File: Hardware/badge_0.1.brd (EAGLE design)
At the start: 100 x 50 mm, 59 parts, among them CON1 PH_2, IC1 CP2102, SW2 MK12C02, U1 SMBT2222A, U2 SMBT2222A, U4 MCP73832T-2DCI/OT

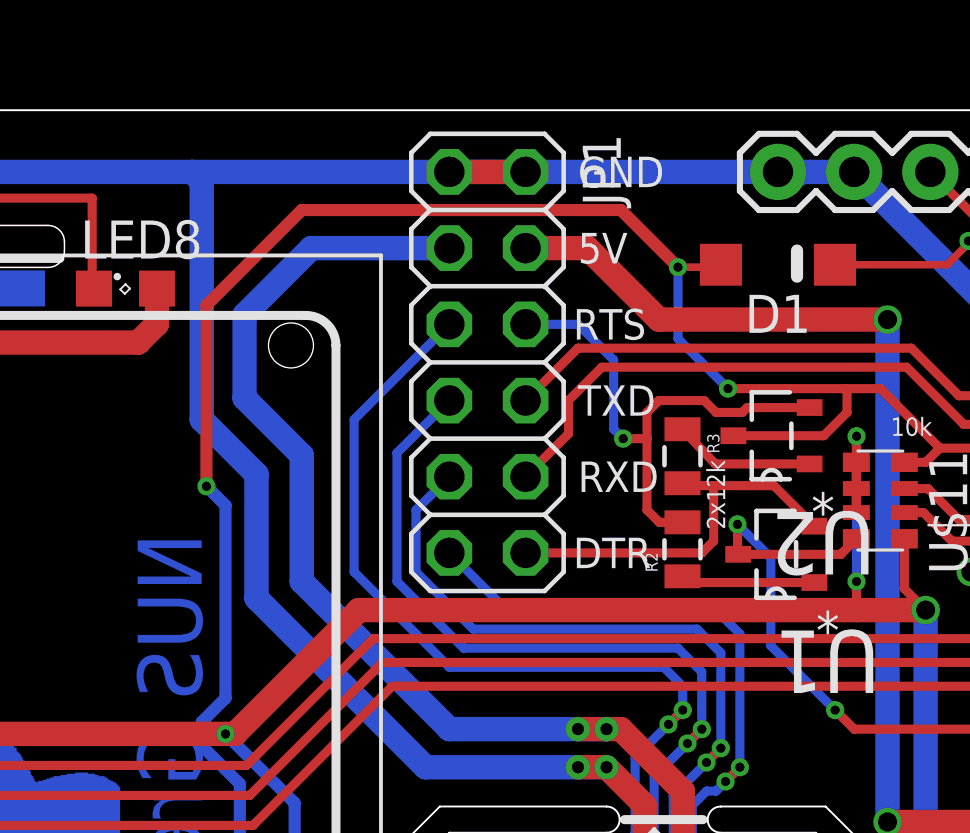
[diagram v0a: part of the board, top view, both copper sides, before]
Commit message: Replaced serial jumpers with a header. Thus removing the need to populate the jumpers during board assembly.
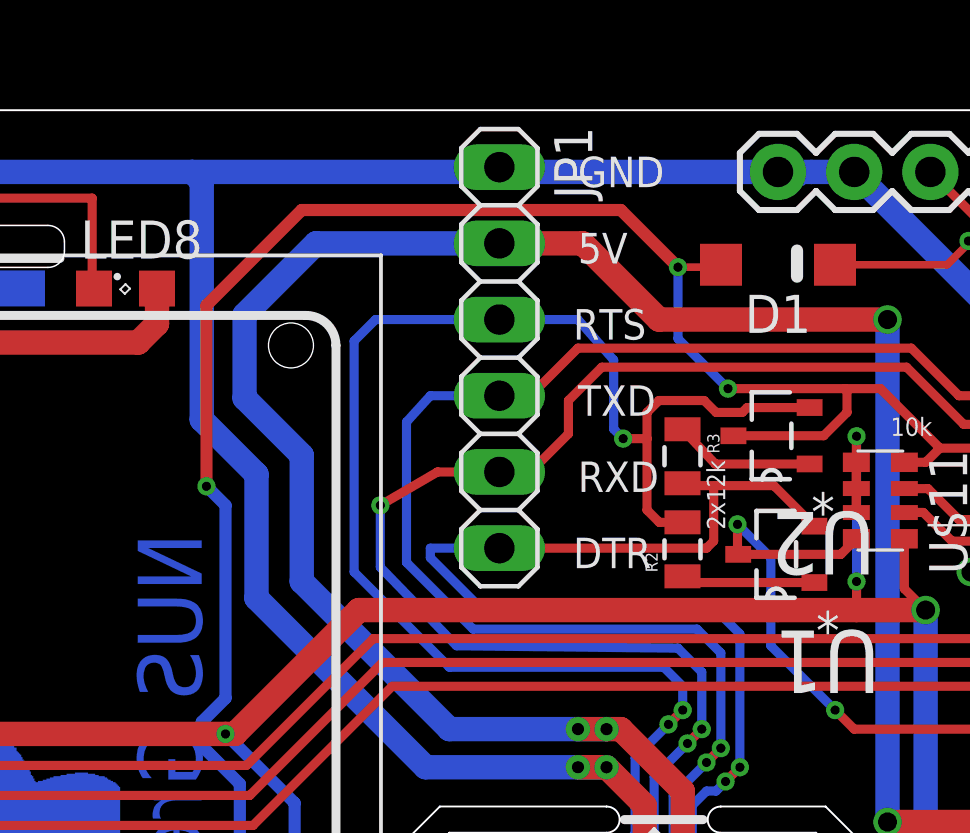
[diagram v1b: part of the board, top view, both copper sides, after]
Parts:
- JP1: device pinhead:2X06 -> pinhead:1X06
- moved JP1 0.43 mm to (45.5, 41.8)
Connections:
- removed net AUTO_DTR: JP1.12, R3.2, U1.2
- removed net AUTO_RTS: JP1.6, R2.2, U2.2
- removed net S_RXD: IC1.25, J2.6, JP1.9
- removed net S_TXD: IC1.26, J2.5, JP1.7
- net 5V: no longer JP1.4
- net GND: no longer JP1.2
- net RX: now also IC1.25, J2.6, JP1.4; no longer JP1.8
- net S_DTR: now also JP1.6, R3.2, U1.2; no longer JP1.11
- net S_RTS: now also JP1.3, R2.2, U2.2; no longer JP1.5
- net TX: now also IC1.26, J2.5, JP1.5; no longer JP1.10
- net VBUS: now also JP1.2; no longer JP1.3
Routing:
- net RX: track 83.3 -> 132.3 mm, vias 3 -> 6
- net TX: track 87.5 -> 134.4 mm, vias 2 -> 6
- net S_TXD: track 45.8 -> 0.00 mm, vias 3 -> 0
- net S_RXD: track 43.2 -> 0.00 mm, vias 3 -> 0
- net S_RTS: track 47.6 -> 69.3 mm, vias 3 -> 4
- net AUTO_RTS: track 17.4 -> 0.00 mm, vias 1 -> 0
- net S_DTR: track 42.0 -> 59.3 mm
- net AUTO_DTR: track 13.3 -> 0.00 mm
- net GND: track 368.0 -> 374.8 mm
- net VBUS: track 69.4 -> 71.1 mm

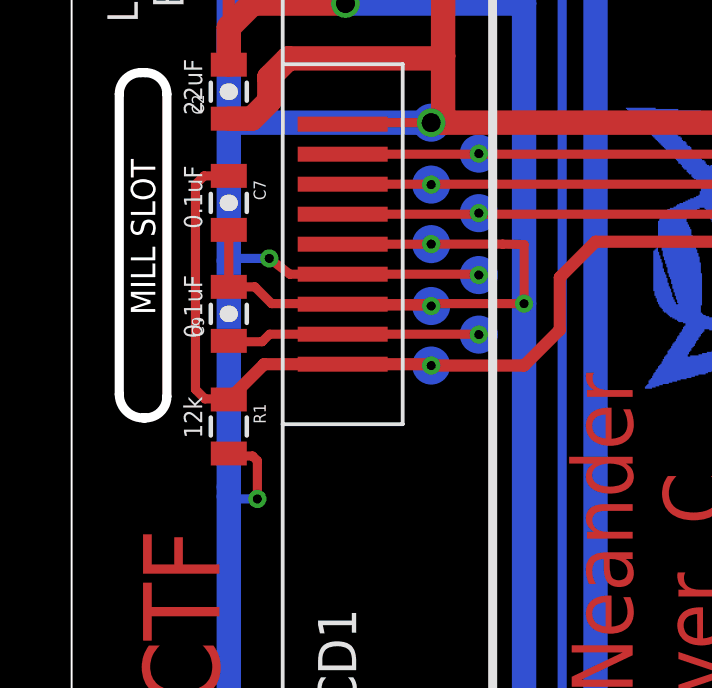
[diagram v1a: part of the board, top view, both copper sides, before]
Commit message: Removed 12K resistor after connecting LCD & ESP resets.
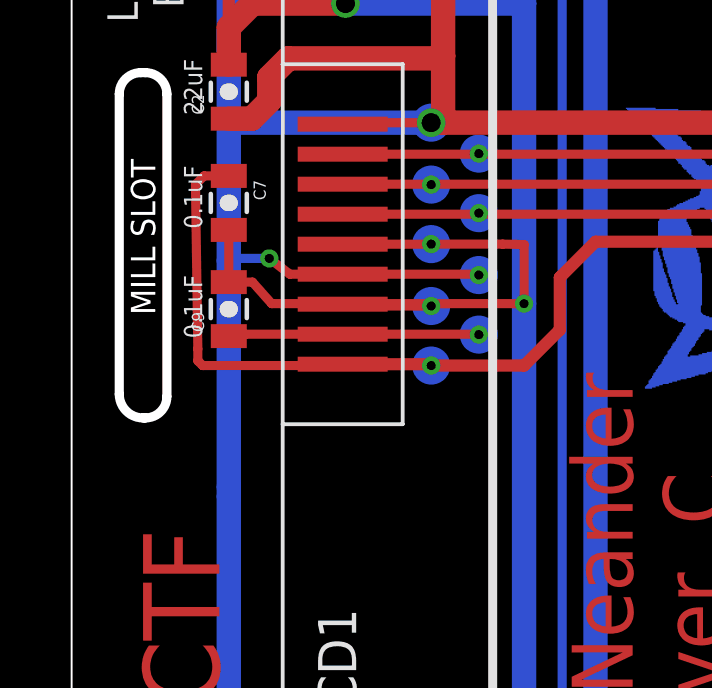
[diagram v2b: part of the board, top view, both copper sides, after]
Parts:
- removed R1: 12K, SparkFun-Passives:0805
- moved C9 0.16 mm to (5.24, 23.0)
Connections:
- net RESET: no longer R1.1
- net VCC: no longer R1.2
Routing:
- net VCC: track 274.4 -> 271.2 mm, vias 12 -> 11
- net RESET: track 156.7 -> 154.8 mm
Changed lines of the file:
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@@
 . ...- . .-. -.-- - .... .. -. --.</text>
 <text x="73.18375" y="42.38625" size="0.6096" layer="21" font="vector" rot="R90" align="center">22uF</text>
-<text x="4.048125" y="20.081875" size="0.6096" layer="21" font="vector" rot="R270" align="center-left">12k</text>
 <text x="52.705" y="38.338125" size="0.6096" layer="21" font="vector" rot="R270" align="center-left">2x12k</text>
 <text x="35.56" y="35.9171875" size="2.1336" layer="30" font="vector" ratio="16" rot="SMR270">NUS Greyhats</text>
@@
 <element name="C4" library="SparkFun-Capacitors" package="0805-CAP" value="10uF" x="63.420625" y="17.700625"/>
 <element name="C5" library="SparkFun-Capacitors" package="0805-CAP" value="10uF" x="63.34125" y="23.8125"/>
-<element name="C9" library="SparkFun-Capacitors" package="0805-CAP" value="100nF" x="5.23875" y="22.8361875" rot="R90"/>
+<element name="C9" library="SparkFun-Capacitors" package="0805-CAP" value="100nF" x="5.23875" y="22.9949375" rot="R90"/>
 <element name="LCD1" library="gm2" package="LPH-7366" value="LPH-7366" x="26.035" y="25.15875" rot="R90"/>
 <element name="U$1" library="badge" package="EVQQWN03W" value="TOUCHSWITCH" x="75.09625" y="14.845625" smashed="yes" rot="R180"/>
@@
 <element name="C6" library="SparkFun-Capacitors" package="0805-CAP" value="10uF" x="74.774375" y="43.38625" rot="R90"/>
 <element name="C7" library="SparkFun-Capacitors" package="0805-CAP" value="100nF" x="5.23875" y="26.5350625" rot="R270"/>
-<element name="R1" library="SparkFun-Passives" package="0805" value="12K" x="5.23875" y="19.08175" rot="R270"/>
 <element name="U1" library="badge" package="SOT95P290X110-3N" value="SMBT2222A" x="54.7131875" y="35.194875" rot="R180">
 <attribute name="MPN" value="SMBT2222A" x="54.7131875" y="35.194875" size="1.778" layer="27" rot="R180" display="off"/>
@@
 <wire x1="76.279375" y1="43.859375" x2="64.690625" y2="43.859375" width="0.8128" layer="16"/>
 <contactref element="LCD1" pad="6"/>
-<contactref element="R1" pad="2"/>
 <contactref element="U$11" pad="5"/>
 <wire x1="58.74375" y1="33.34375" x2="58.7375" y2="33.3375" width="0.3048" layer="1"/>
@@
 <via x="57.388125" y="34.29" extent="1-16" drill="0.3048" shape="octagon"/>
 <wire x1="57.388125" y1="34.29" x2="57.388125" y2="33.3375" width="0.3048" layer="1"/>
-<via x="6.19125" y="16.66875" extent="1-16" drill="0.3048" shape="octagon"/>
 <via x="6.588125" y="24.685625" extent="1-16" drill="0.3048" shape="octagon"/>
 <contactref element="TP3" pad="TP"/>
@@
 <wire x1="73.09625" y1="17.645625" x2="73.09625" y2="20.645625" width="0.8128" layer="1"/>
 <wire x1="5.3975" y1="17.224375" x2="5.23875" y2="17.065625" width="0.3048" layer="16"/>
-<wire x1="6.19125" y1="16.66875" x2="5.318125" y2="16.66875" width="0.3048" layer="16"/>
 <wire x1="5.318125" y1="16.66875" x2="5.23875" y2="16.748125" width="0.3048" layer="16"/>
-<wire x1="6.19125" y1="17.93875" x2="6.19125" y2="16.66875" width="0.3048" layer="1"/>
 <wire x1="9.035" y1="24.15875" x2="7.27375" y2="24.15875" width="0.3048" layer="1"/>
 <wire x1="7.27375" y1="24.15875" x2="6.588125" y2="24.685625" width="0.3048" layer="1"/>
 <wire x1="6.588125" y1="24.685625" x2="5.318125" y2="24.685625" width="0.3048" layer="16"/>
 <wire x1="5.318125" y1="24.685625" x2="5.23875" y2="24.60625" width="0.3048" layer="16"/>
-<wire x1="5.5055625" y1="18.0975" x2="5.23875" y2="18.18175" width="0.3048" layer="1"/>
-<wire x1="5.5055625" y1="18.0975" x2="6.0325" y2="18.0975" width="0.3048" layer="1"/>
-<wire x1="6.0325" y1="18.0975" x2="6.19125" y2="17.93875" width="0.3048" layer="1"/>
 <contactref element="C2" pad="1"/>
 <wire x1="5.23875" y1="29.341875" x2="6.005625" y2="29.341875" width="0.8128" layer="1"/>
@@
 <wire x1="84.96625" y1="9.728125" x2="79.36625" y2="9.728125" width="0.6096" layer="1"/>
 <wire x1="9.01625" y1="23.1775" x2="6.6675" y2="23.1775" width="0.3048" layer="1"/>
-<wire x1="6.6675" y1="23.1775" x2="6.1088125" y2="23.7361875" width="0.3048" layer="1"/>
-<wire x1="6.1088125" y1="23.7361875" x2="5.23875" y2="23.7361875" width="0.3048" layer="1"/>
-<wire x1="5.23875" y1="25.6350625" x2="5.23875" y2="23.7361875" width="0.3048" layer="1"/>
+<wire x1="6.6675" y1="23.1775" x2="6.0294375" y2="23.8949375" width="0.3048" layer="1"/>
+<wire x1="6.0294375" y1="23.8949375" x2="5.23875" y2="23.8949375" width="0.3048" layer="1"/>
+<wire x1="5.23875" y1="25.6350625" x2="5.23875" y2="23.8949375" width="0.3048" layer="1"/>
 <wire x1="35.56" y1="47.625" x2="35.56" y2="39.6875" width="0.8128" layer="16"/>
 <wire x1="35.56" y1="39.6875" x2="37.385625" y2="37.861875" width="0.8128" layer="16"/>
@@
 <wire x1="53.101875" y1="40.719375" x2="51.435" y2="42.38625" width="0.3048" layer="16"/>
 <wire x1="51.435" y1="42.38625" x2="51.435" y2="44.7675" width="0.3048" layer="16"/>
-<contactref element="R1" pad="1"/>
 <contactref element="C7" pad="1"/>
 <contactref element="LCD1" pad="9"/>
@@
 <wire x1="5.23875" y1="27.4350625" x2="4.4163125" y2="27.4350625" width="0.3048" layer="1"/>
 <wire x1="4.4163125" y1="27.4350625" x2="4.1275" y2="27.14625" width="0.3048" layer="1"/>
-<wire x1="4.1275" y1="27.14625" x2="4.1275" y2="20.32" width="0.3048" layer="1"/>
-<wire x1="4.1275" y1="20.32" x2="4.445" y2="20.0025" width="0.3048" layer="1"/>
-<wire x1="4.445" y1="20.0025" x2="5.4005625" y2="20.0025" width="0.3048" layer="1"/>
-<wire x1="5.4005625" y1="20.0025" x2="5.23875" y2="19.98175" width="0.3048" layer="1"/>
+<wire x1="4.1275" y1="27.14625" x2="4.206875" y2="21.669375" width="0.3048" layer="1"/>
 <wire x1="9.035" y1="21.15875" x2="11.940625" y2="21.15875" width="0.4064" layer="1"/>
 <wire x1="11.940625" y1="21.15875" x2="11.985625" y2="21.11375" width="0.4064" layer="1"/>
@@
 <wire x1="57.070625" y1="39.925625" x2="57.070625" y2="40.64" width="0.3048" layer="1"/>
 <wire x1="57.070625" y1="40.64" x2="56.99125" y2="40.719375" width="0.3048" layer="1"/>
-<wire x1="9.035" y1="21.15875" x2="6.41575" y2="21.15875" width="0.4064" layer="1"/>
-<wire x1="6.41575" y1="21.15875" x2="5.23875" y2="19.98175" width="0.4064" layer="1"/>
 <wire x1="11.985625" y1="21.11375" x2="15.08125" y2="21.11375" width="0.4064" layer="1"/>
 <wire x1="15.08125" y1="21.11375" x2="16.271875" y2="22.304375" width="0.4064" layer="1"/>
@@
 <wire x1="36.83" y1="25.24125" x2="36.83" y2="27.543125" width="0.4064" layer="16"/>
 <wire x1="91.38609375" y1="42.5503125" x2="91.38609375" y2="43.4" width="0.4064" layer="1"/>
+<wire x1="4.206875" y1="21.669375" x2="4.206875" y2="21.2725" width="0.3048" layer="1"/>
+<wire x1="4.206875" y1="21.2725" x2="4.365625" y2="21.11375" width="0.3048" layer="1"/>
+<wire x1="4.365625" y1="21.11375" x2="8.99" y2="21.11375" width="0.3048" layer="1"/>
+<wire x1="8.99" y1="21.11375" x2="9.035" y2="21.15875" width="0.3048" layer="1"/>
 </signal>
 <signal name="ADC">
@@
 <wire x1="9.035" y1="22.15875" x2="13.56" y2="22.15875" width="0.3048" layer="1"/>
 <wire x1="13.56" y1="22.15875" x2="13.573125" y2="22.145625" width="0.3048" layer="1"/>
-<wire x1="9.035" y1="22.15875" x2="6.60125" y2="22.15875" width="0.3048" layer="1"/>
-<wire x1="6.60125" y1="22.15875" x2="6.35" y2="21.9075" width="0.3048" layer="1"/>
-<wire x1="6.35" y1="21.9075" x2="5.45" y2="21.9075" width="0.3048" layer="1"/>
-<wire x1="5.45" y1="21.9075" x2="5.23875" y2="21.9361875" width="0.3048" layer="1"/>
+<wire x1="9.035" y1="22.15875" x2="5.8075" y2="22.15875" width="0.3048" layer="1"/>
+<wire x1="5.8075" y1="22.15875" x2="5.55625" y2="22.145625" width="0.3048" layer="1"/>
+<wire x1="5.55625" y1="22.145625" x2="5.45" y2="22.145625" width="0.3048" layer="1"/>
+<wire x1="5.45" y1="22.145625" x2="5.23875" y2="22.0949375" width="0.3048" layer="1"/>
 </signal>
 <signal name="N$11">

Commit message: electrons fell out
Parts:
- moved C6 0.40 mm to (74.4, 43.4)
- moved IC1 0.40 mm to (51.7, 12.6)
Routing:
- net GND: track 374.8 -> 382.6 mm
- net VBUS: track 71.1 -> 77.6 mm
- net VCC: track 271.2 -> 274.6 mm
- net GPIO5: track 39.1 -> 42.3 mm
- net S_DTR: track 59.3 -> 56.5 mm, vias 3 -> 2
- net TX: track 134.4 -> 132.2 mm, vias 6 -> 5
- net S_RTS: track 69.3 -> 67.3 mm, vias 4 -> 3
- net RX: track 132.3 -> 130.7 mm
- net GPIO2/SDA: track 69.9 -> 71.3 mm
- net S_CTS: track 14.4 -> 13.0 mm
- net GPIO16: track 35.0 -> 36.2 mm
- net N$8: track 13.3 -> 12.6 mm
- net RESET: track 154.8 -> 154.1 mm
- net MOSI: track 24.8 -> 24.1 mm
- net GPIO14/SPI_CLK/SCL: track 98.7 -> 98.0 mm
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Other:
- board text added: "220R"
- board text removed: "100R"

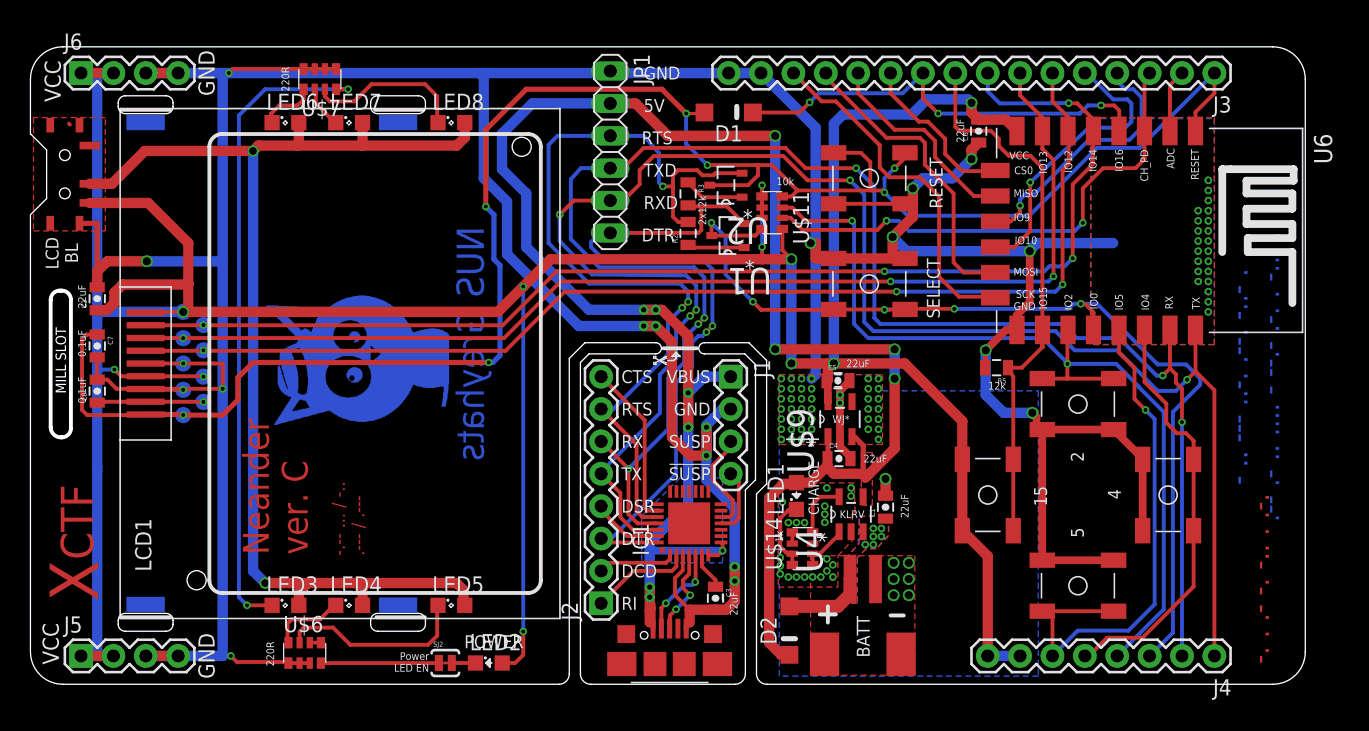
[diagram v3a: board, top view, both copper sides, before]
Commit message: moved pads and vias out of the way
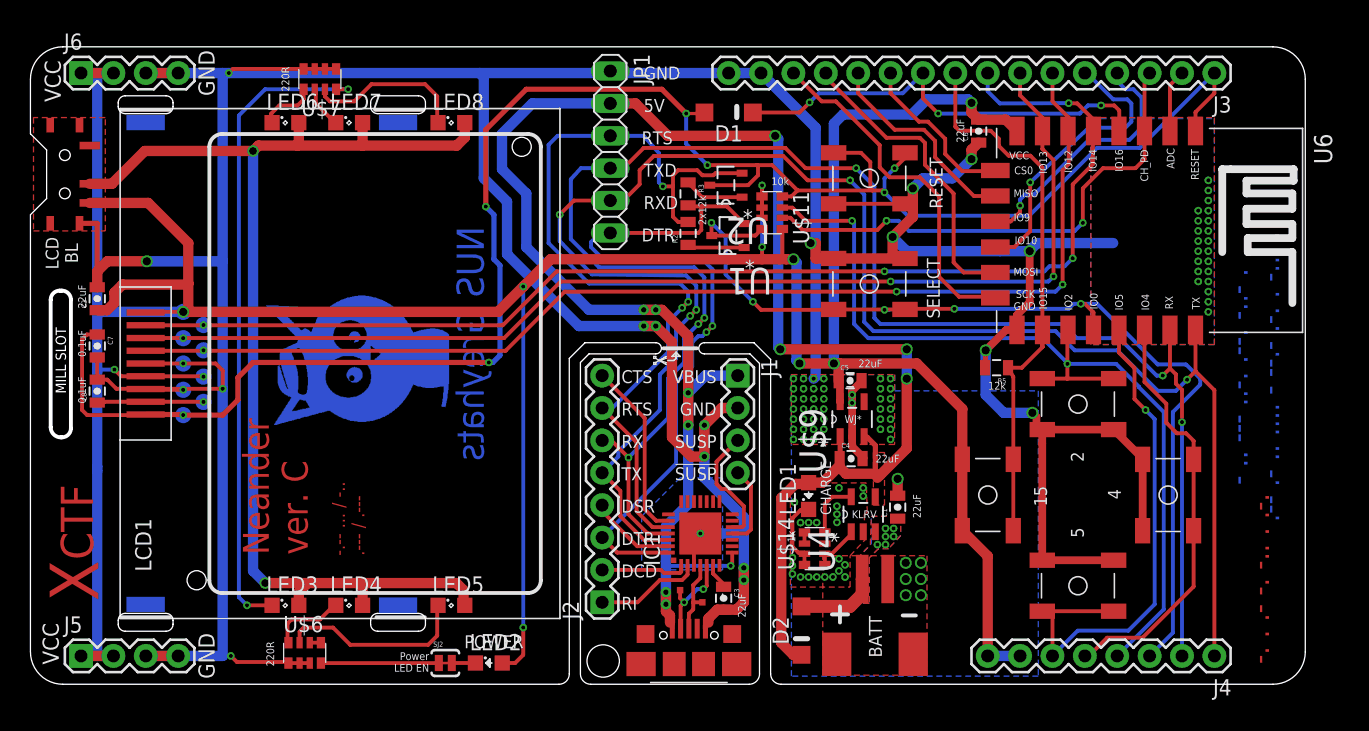
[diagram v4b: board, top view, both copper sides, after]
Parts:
- added TP10, TP11: TEST-POINT2, SparkFun-Passives:PAD.02X.02
- moved U$10 1.51 mm to (51.6, 1.59)
- moved IC1 1.18 mm to (52.5, 11.8)
- moved C1 0.95 mm to (68.0, 13.9)
- moved C4 0.95 mm to (64.4, 17.7)
- moved C5 0.95 mm to (64.3, 23.8)
- moved CON1 0.95 mm to (66.2, 8.26)
- moved D2 0.95 mm to (60.5, 4.21)
- moved LED1 0.95 mm to (61.0, 14.8)
- moved U$14 0.95 mm to (61.5, 10.6)
- moved U$9 0.95 mm to (64.5, 20.8)
- moved U4 0.95 mm to (65.3, 13.3)
- moved C3 0.64 mm to (54.4, 6.75)
- moved J1 0.56 mm to (55.5, 24.2)
- moved J2 0.11 mm to (44.8, 6.43)
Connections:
- net D+: now also TP11.P$1
- net D-: now also TP10.P$1
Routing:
- net VBUS: track 77.6 -> 73.7 mm
- net GND: track 382.6 -> 381.0 mm, vias 112 -> 113
- net S_SUSP: track 7.97 -> 9.45 mm
- net S_DSR: track 5.56 -> 6.81 mm
- net S_RTS: track 67.3 -> 68.5 mm
- net S_!SUSP: track 5.31 -> 6.47 mm
- net TX: track 132.2 -> 133.2 mm
- net S_CTS: track 13.0 -> 14.1 mm
- net D+: track 7.00 -> 6.05 mm, vias 2 -> 0
- net N$20: track 2.91 -> 2.02 mm
- net RX: track 130.7 -> 131.5 mm
- net VCC: track 274.6 -> 275.4 mm
- net S_DCD: track 6.07 -> 6.84 mm
- net 5V: track 79.9 -> 80.6 mm
- net S_DTR: track 56.5 -> 57.1 mm
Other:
- outline, holes or cut-outs redrawn
- board text added: "USB TTL"
- board text removed: "USB-TTL"

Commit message: dunno what I did
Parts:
- moved R5 0.40 mm to (76.2, 24.8)
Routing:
- net GPIO15/SPI_CS: track 44.8 -> 44.2 mm
